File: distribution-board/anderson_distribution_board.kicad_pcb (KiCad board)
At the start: 2 copper layers, 65 x 20 mm, 5 parts, among them J1 Anderson_two_redblack, J2 Anderson_two_redblack, J3 Anderson_two_redblack, J4 Anderson_two_redblack, J5 Anderson_two_redblack

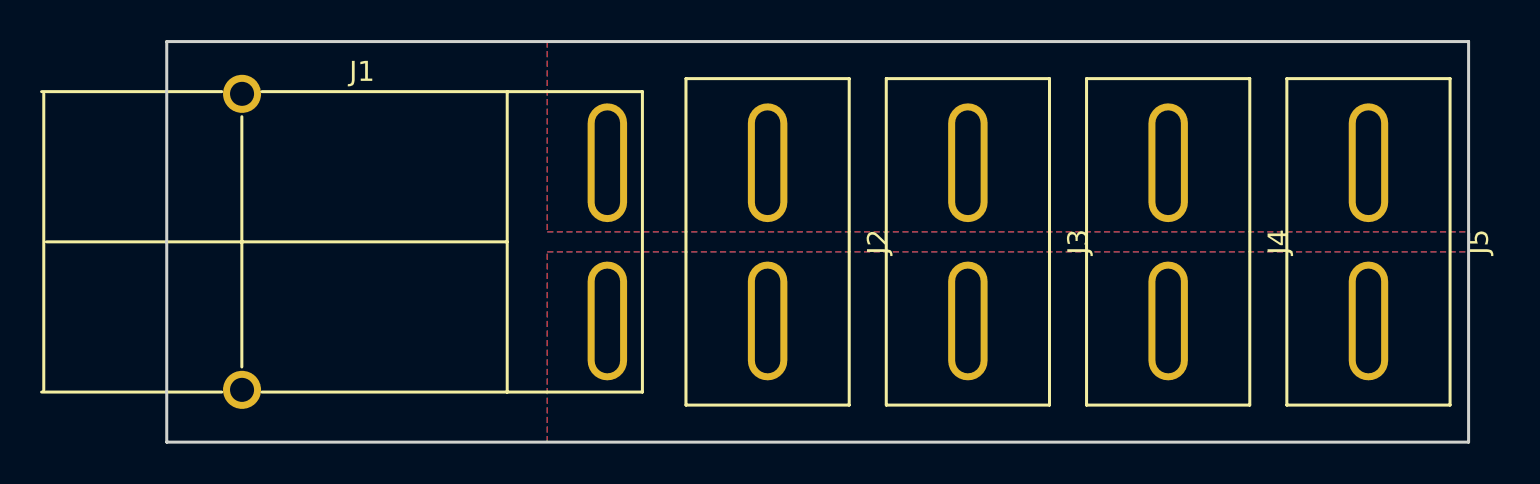
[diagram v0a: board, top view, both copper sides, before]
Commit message: Distribution board v1.1:
- Fix silk on anderson connectors
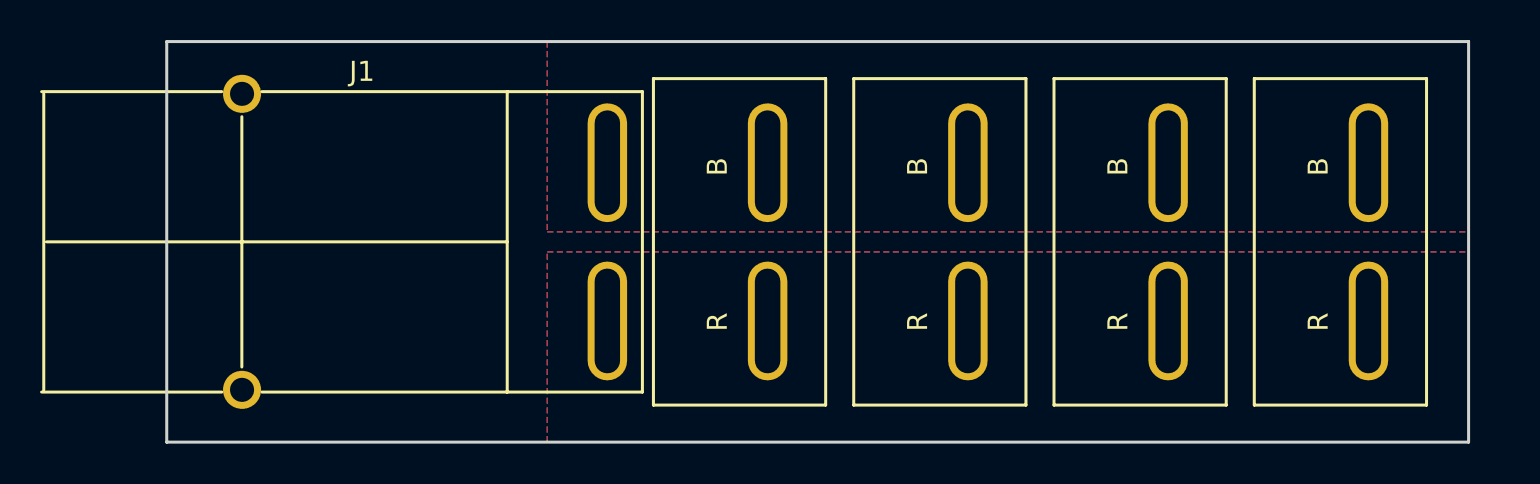
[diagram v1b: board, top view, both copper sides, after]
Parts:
- J2, J3, J4, J5: footprint homebrew:Anderson_1337G3_straight_two -> homebrew:Anderson_1335G1_straight_two
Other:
- board text added: "v1.1"
- board text removed: "v1.0"
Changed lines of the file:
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@@
-(kicad_pcb (version 4) (host pcbnew 4.0.6+dfsg1-1)
+(kicad_pcb (version 20171130) (host pcbnew 5.1.5-52549c5~84~ubuntu18.04.1)
   (general
-    (links 8)
-    (no_connects 0)
-    (area 79.224999 66.924999 156.575 89.075)
     (thickness 1.6)
     (drawings 5)
@@
     (zone_45_only no)
     (trace_min 0.2)
-    (segment_width 0.2)
-    (edge_width 0.15)
     (via_size 0.6)
     (via_drill 0.4)
@@
     (uvia_min_size 0.2)
     (uvia_min_drill 0.1)
+    (edge_width 0.15)
+    (segment_width 0.2)
     (pcb_text_width 0.3)
     (pcb_text_size 1.5 1.5)
@@
       (layerselection 0x3f0f0_80000001)
       (usegerberextensions false)
+      (usegerberattributes false)
+      (usegerberadvancedattributes false)
+      (creategerberjobfile false)
       (excludeedgelayer true)
       (linewidth 0.100000)
@@
       (hpglpennumber 1)
       (hpglpenspeed 20)
-      (hpglpendiameter 15)
-      (hpglpenoverlay 2)
+      (hpglpendiameter 15.000000)
       (psnegative false)
       (psa4output false)
@@
     (add_net "Net-(J1-Pad1)")
     (add_net "Net-(J1-Pad2)")
+  )
+  (module homebrew:Anderson_1335G1_straight_two (layer F.Cu)
+    (at 150 77 90)
+    (fp_text reference J5 (at 0 3.75 90) (layer F.SilkS) hide
+      (effects (font (size 1 1) (thickness 0.15)))
+    )
+    (fp_text value Anderson_two_redblack (at 0 -6.45 270) (layer F.Fab)
+      (effects (font (size 1 1) (thickness 0.15)))
+    )
+    (fp_text user B (at 3.75 -2.5 90) (layer F.SilkS)
+      (effects (font (size 1 1) (thickness 0.15)))
+    )
+    (fp_line (start -8.15 -5.7) (end 8.15 -5.7) (layer F.SilkS) (width 0.15))
+    (fp_line (start -8.15 2.9) (end -8.15 -5.7) (layer F.SilkS) (width 0.15))
+    (fp_line (start 8.15 2.9) (end -8.15 2.9) (layer F.SilkS) (width 0.15))
+    (fp_line (start 8.15 -5.7) (end 8.15 2.9) (layer F.SilkS) (width 0.15))
+    (fp_text user R (at -4 -2.5 90) (layer F.SilkS)
+      (effects (font (size 1 1) (thickness 0.15)))
+    )
+    (pad 2 thru_hole oval (at 3.95 0 90) (size 5.93 1.97) (drill oval 5.23 1.27) (layers *.Cu *.Mask)
+      (net 2 "Net-(J1-Pad2)"))
+    (pad 1 thru_hole oval (at -3.95 0 90) (size 5.93 1.97) (drill oval 5.23 1.27) (layers *.Cu *.Mask)
+      (net 1 "Net-(J1-Pad1)"))
+  )
+  (module homebrew:Anderson_1335G1_straight_two (layer F.Cu)
+    (at 140 77 90)
+    (fp_text reference J4 (at 0 3.75 90) (layer F.SilkS) hide
+      (effects (font (size 1 1) (thickness 0.15)))
+    )
+    (fp_text value Anderson_two_redblack (at 0 -6.45 270) (layer F.Fab)
+      (effects (font (size 1 1) (thickness 0.15)))
+    )
+    (fp_text user B (at 3.75 -2.5 90) (layer F.SilkS)
+      (effects (font (size 1 1) (thickness 0.15)))
+    )
+    (fp_line (start -8.15 -5.7) (end 8.15 -5.7) (layer F.SilkS) (width 0.15))
+    (fp_line (start -8.15 2.9) (end -8.15 -5.7) (layer F.SilkS) (width 0.15))
+    (fp_line (start 8.15 2.9) (end -8.15 2.9) (layer F.SilkS) (width 0.15))
+    (fp_line (start 8.15 -5.7) (end 8.15 2.9) (layer F.SilkS) (width 0.15))
+    (fp_text user R (at -4 -2.5 90) (layer F.SilkS)
+      (effects (font (size 1 1) (thickness 0.15)))
+    )
+    (pad 2 thru_hole oval (at 3.95 0 90) (size 5.93 1.97) (drill oval 5.23 1.27) (layers *.Cu *.Mask)
+      (net 2 "Net-(J1-Pad2)"))
+    (pad 1 thru_hole oval (at -3.95 0 90) (size 5.93 1.97) (drill oval 5.23 1.27) (layers *.Cu *.Mask)
+      (net 1 "Net-(J1-Pad1)"))
+  )
+  (module homebrew:Anderson_1335G1_straight_two (layer F.Cu)
+    (at 130 77 90)
+    (fp_text reference J3 (at 0 3.75 90) (layer F.SilkS) hide
+      (effects (font (size 1 1) (thickness 0.15)))
+    )
+    (fp_text value Anderson_two_redblack (at 0 -6.45 270) (layer F.Fab)
+      (effects (font (size 1 1) (thickness 0.15)))
+    )
+    (fp_text user B (at 3.75 -2.5 90) (layer F.SilkS)
+      (effects (font (size 1 1) (thickness 0.15)))
+    )
+    (fp_line (start -8.15 -5.7) (end 8.15 -5.7) (layer F.SilkS) (width 0.15))
+    (fp_line (start -8.15 2.9) (end -8.15 -5.7) (layer F.SilkS) (width 0.15))
+    (fp_line (start 8.15 2.9) (end -8.15 2.9) (layer F.SilkS) (width 0.15))
+    (fp_line (start 8.15 -5.7) (end 8.15 2.9) (layer F.SilkS) (width 0.15))
+    (fp_text user R (at -4 -2.5 90) (layer F.SilkS)
+      (effects (font (size 1 1) (thickness 0.15)))
+    )
+    (pad 2 thru_hole oval (at 3.95 0 90) (size 5.93 1.97) (drill oval 5.23 1.27) (layers *.Cu *.Mask)
+      (net 2 "Net-(J1-Pad2)"))
+    (pad 1 thru_hole oval (at -3.95 0 90) (size 5.93 1.97) (drill oval 5.23 1.27) (layers *.Cu *.Mask)
+      (net 1 "Net-(J1-Pad1)"))
+  )
+  (module homebrew:Anderson_1335G1_straight_two (layer F.Cu)
+    (at 120 77 90)
+    (fp_text reference J2 (at 0 3.75 90) (layer F.SilkS) hide
+      (effects (font (size 1 1) (thickness 0.15)))
+    )
+    (fp_text value Anderson_two_redblack (at 0 -6.45 270) (layer F.Fab)
+      (effects (font (size 1 1) (thickness 0.15)))
+    )
+    (fp_text user B (at 3.75 -2.5 90) (layer F.SilkS)
+      (effects (font (size 1 1) (thickness 0.15)))
+    )
+    (fp_line (start -8.15 -5.7) (end 8.15 -5.7) (layer F.SilkS) (width 0.15))
+    (fp_line (start -8.15 2.9) (end -8.15 -5.7) (layer F.SilkS) (width 0.15))
+    (fp_line (start 8.15 2.9) (end -8.15 2.9) (layer F.SilkS) (width 0.15))
+    (fp_line (start 8.15 -5.7) (end 8.15 2.9) (layer F.SilkS) (width 0.15))
+    (fp_text user R (at -4 -2.5 90) (layer F.SilkS)
+      (effects (font (size 1 1) (thickness 0.15)))
+    )
+    (pad 2 thru_hole oval (at 3.95 0 90) (size 5.93 1.97) (drill oval 5.23 1.27) (layers *.Cu *.Mask)
+      (net 2 "Net-(J1-Pad2)"))
+    (pad 1 thru_hole oval (at -3.95 0 90) (size 5.93 1.97) (drill oval 5.23 1.27) (layers *.Cu *.Mask)
+      (net 1 "Net-(J1-Pad1)"))
   )
   (module homebrew:Anderson_1337G3_right_angle_bottom_two (layer F.Cu)
@@
     (pad "" thru_hole circle (at 7.39 -18.24 90) (size 1.9 1.9) (drill 1.2) (layers *.Cu *.Mask))
   )
-  (module homebrew:Anderson_1337G3_straight_two (layer F.Cu)
-    (at 120 77 90)
-    (fp_text reference J2 (at 0 5.5 270) (layer F.SilkS)
-      (effects (font (size 1 1) (thickness 0.15)))
-    )
-    (fp_text value Anderson_two_redblack (at 0.5 -5.25 270) (layer F.Fab)
-      (effects (font (size 1 1) (thickness 0.15)))
-    )
-    (fp_line (start 8.15 -4.075) (end 8.15 4.075) (layer F.SilkS) (width 0.15))
-    (fp_line (start 8.15 4.075) (end -8.15 4.075) (layer F.SilkS) (width 0.15))
-    (fp_line (start -8.15 4.075) (end -8.15 -4.075) (layer F.SilkS) (width 0.15))
-    (fp_line (start -8.15 -4.075) (end 8.15 -4.075) (layer F.SilkS) (width 0.15))
-    (pad 1 thru_hole oval (at -3.95 0 90) (size 5.93 1.97) (drill oval 5.23 1.27) (layers *.Cu *.Mask)
-      (net 1 "Net-(J1-Pad1)"))
-    (pad 2 thru_hole oval (at 3.95 0 90) (size 5.93 1.97) (drill oval 5.23 1.27) (layers *.Cu *.Mask)
-      (net 2 "Net-(J1-Pad2)"))
-  )
-  (module homebrew:Anderson_1337G3_straight_two (layer F.Cu)
-    (at 130 77 90)
-    (fp_text reference J3 (at 0 5.5 270) (layer F.SilkS)
-      (effects (font (size 1 1) (thickness 0.15)))
-    )
-    (fp_text value Anderson_two_redblack (at 0.5 -5.25 270) (layer F.Fab)
-      (effects (font (size 1 1) (thickness 0.15)))
-    )
-    (fp_line (start 8.15 -4.075) (end 8.15 4.075) (layer F.SilkS) (width 0.15))
-    (fp_line (start 8.15 4.075) (end -8.15 4.075) (layer F.SilkS) (width 0.15))
-    (fp_line (start -8.15 4.075) (end -8.15 -4.075) (layer F.SilkS) (width 0.15))
-    (fp_line (start -8.15 -4.075) (end 8.15 -4.075) (layer F.SilkS) (width 0.15))
-    (pad 1 thru_hole oval (at -3.95 0 90) (size 5.93 1.97) (drill oval 5.23 1.27) (layers *.Cu *.Mask)
-      (net 1 "Net-(J1-Pad1)"))
-    (pad 2 thru_hole oval (at 3.95 0 90) (size 5.93 1.97) (drill oval 5.23 1.27) (layers *.Cu *.Mask)
-      (net 2 "Net-(J1-Pad2)"))
-  )
-  (module homebrew:Anderson_1337G3_straight_two (layer F.Cu)
-    (at 140 77 90)
-    (fp_text reference J4 (at 0 5.5 270) (layer F.SilkS)
-      (effects (font (size 1 1) (thickness 0.15)))
-    )
-    (fp_text value Anderson_two_redblack (at 0.5 -5.25 270) (layer F.Fab)
-      (effects (font (size 1 1) (thickness 0.15)))
-    )
-    (fp_line (start 8.15 -4.075) (end 8.15 4.075) (layer F.SilkS) (width 0.15))
-    (fp_line (start 8.15 4.075) (end -8.15 4.075) (layer F.SilkS) (width 0.15))
-    (fp_line (start -8.15 4.075) (end -8.15 -4.075) (layer F.SilkS) (width 0.15))
-    (fp_line (start -8.15 -4.075) (end 8.15 -4.075) (layer F.SilkS) (width 0.15))
-    (pad 1 thru_hole oval (at -3.95 0 90) (size 5.93 1.97) (drill oval 5.23 1.27) (layers *.Cu *.Mask)
-      (net 1 "Net-(J1-Pad1)"))
-    (pad 2 thru_hole oval (at 3.95 0 90) (size 5.93 1.97) (drill oval 5.23 1.27) (layers *.Cu *.Mask)
-      (net 2 "Net-(J1-Pad2)"))
-  )
-  (module homebrew:Anderson_1337G3_straight_two (layer F.Cu)
-    (at 150 77 90)
-    (fp_text reference J5 (at 0 5.5 270) (layer F.SilkS)
-      (effects (font (size 1 1) (thickness 0.15)))
-    )
-    (fp_text value Anderson_two_redblack (at 0.5 -5.25 270) (layer F.Fab)
-      (effects (font (size 1 1) (thickness 0.15)))
-    )
-    (fp_line (start 8.15 -4.075) (end 8.15 4.075) (layer F.SilkS) (width 0.15))
-    (fp_line (start 8.15 4.075) (end -8.15 4.075) (layer F.SilkS) (width 0.15))
-    (fp_line (start -8.15 4.075) (end -8.15 -4.075) (layer F.SilkS) (width 0.15))
-    (fp_line (start -8.15 -4.075) (end 8.15 -4.075) (layer F.SilkS) (width 0.15))
-    (pad 1 thru_hole oval (at -3.95 0 90) (size 5.93 1.97) (drill oval 5.23 1.27) (layers *.Cu *.Mask)
-      (net 1 "Net-(J1-Pad1)"))
-    (pad 2 thru_hole oval (at 3.95 0 90) (size 5.93 1.97) (drill oval 5.23 1.27) (layers *.Cu *.Mask)
-      (net 2 "Net-(J1-Pad2)"))
-  )
-  (gr_text v1.0 (at 101.5 77 90) (layer B.SilkS)
+  (gr_text v1.1 (at 101.5 77 90) (layer B.SilkS)
     (effects (font (size 4 4) (thickness 0.7)) (justify mirror))
   )

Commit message: distribution-board v1.2:
- Update straight Anderson footprint for fixed silk, bigger copper ring
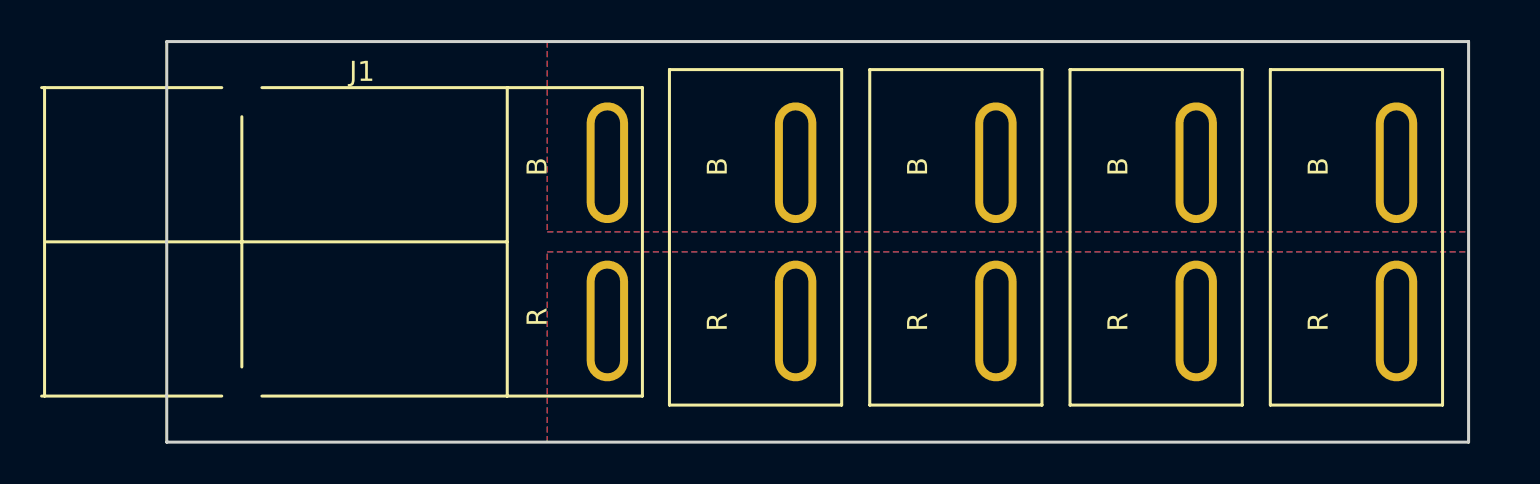
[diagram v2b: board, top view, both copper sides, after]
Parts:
- J1: footprint homebrew:Anderson_1337G3_right_angle_bottom_two -> homebrew:Anderson_1336G1_right_angle_bottom_two
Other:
- board text added: "v1.2"
- board text removed: "v1.1"
